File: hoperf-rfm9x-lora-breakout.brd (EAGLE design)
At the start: 26 x 22.5 mm, 6 parts, among them U1 HopeRF-RFM9x

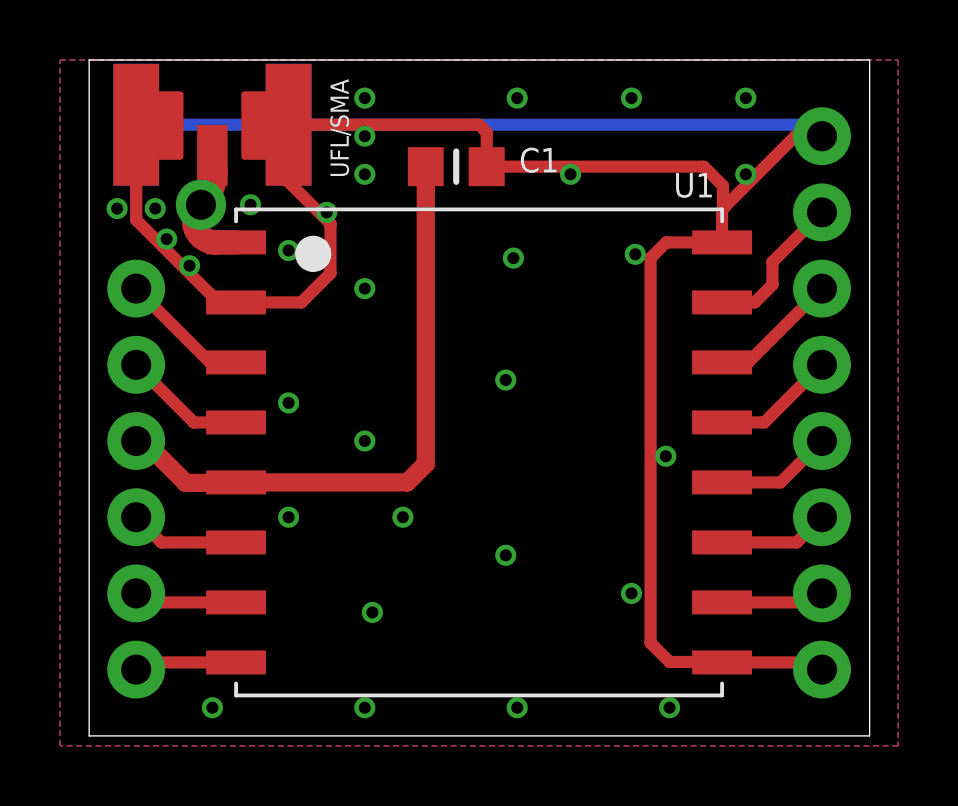
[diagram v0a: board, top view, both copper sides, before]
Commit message: rfm9x lora breakout v1.1
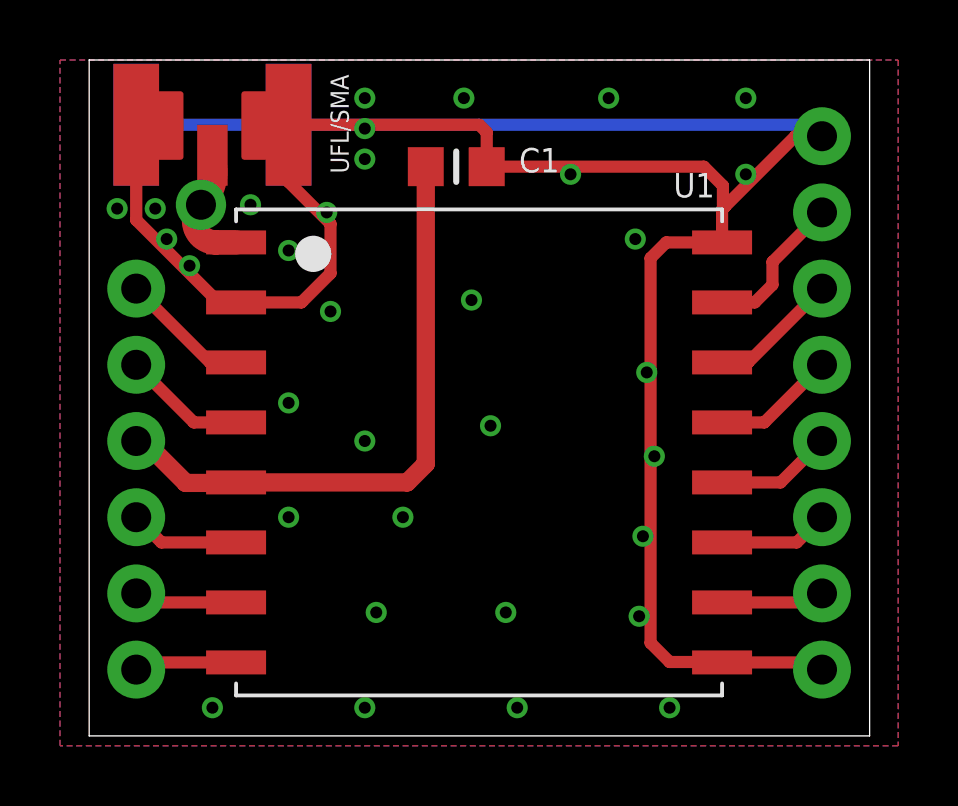
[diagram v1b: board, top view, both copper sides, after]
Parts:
- added LOGO1: OSHW-LOGOS, SparkFun-Aesthetics:OSHW-LOGO-S
- added U$3: LORA_LOGO, #afb-Aesthetics:LORA_LOGO
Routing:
- net GND: vias 31 -> 33
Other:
- board text added: "ANT"
- board text added: "Freq: 315 ( ) 433 ( ) 868 ( ) 915 ( )"
- board text added: "github.com/altro-id"
- board text removed: "Freq: 433 ( ) 868 ( ) 915 ( )"
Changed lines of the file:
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@@
 <setting verticaltext="up"/>
 </settings>
-<grid distance="0.025" unitdist="inch" unit="inch" style="lines" multiple="1" display="no" altdistance="0.025" altunitdist="inch" altunit="inch"/>
+<grid distance="0.005" unitdist="inch" unit="inch" style="lines" multiple="1" display="no" altdistance="0.025" altunitdist="inch" altunit="inch"/>
 <layers>
 <layer number="1" name="Top" color="4" fill="1" visible="yes" active="yes"/>
@@
 <wire x1="0.9725" y1="0.33" x2="26.9875" y2="0.33" width="0" layer="20"/>
 <wire x1="26.9875" y1="0.33" x2="26.9875" y2="22.86" width="0" layer="20"/>
-<text x="19.558" y="13.081" size="0.8128" layer="26" font="vector" ratio="18" rot="MR0">HopeRF-RFM9x
+<text x="18.288" y="12.065" size="0.8128" layer="26" font="vector" ratio="18" rot="MR0">HopeRF-RFM9x
 LoRa Module</text>
-<text x="19.558" y="8.001" size="0.8128" layer="26" font="vector" ratio="18" rot="MR0">Freq:
+<text x="18.288" y="5.207" size="0.8128" layer="26" font="vector" ratio="18" rot="MR0">Freq:
+315 (  )
 433 (  )
 868 (  )
 915 (  )</text>
-<text x="-1.27" y="15.24" size="1.27" layer="103" align="center-right">DIO3</text>
-<text x="-1.27" y="12.7" size="1.27" layer="103" align="center-right">DIO4</text>
-<text x="-1.27" y="10.16" size="1.27" layer="103" align="center-right">+3.3V</text>
-<text x="-1.27" y="7.62" size="1.27" layer="103" align="center-right">DIO0</text>
-<text x="-1.27" y="5.08" size="1.27" layer="103" align="center-right">DIO1</text>
-<text x="-1.27" y="2.54" size="1.27" layer="103" align="center-right">DIO2</text>
-<text x="29.21" y="20.32" size="1.27" layer="103" rot="R180" align="center-right">GND</text>
-<text x="29.21" y="17.78" size="1.27" layer="103" rot="R180" align="center-right">DIO5</text>
-<text x="29.21" y="15.24" size="1.27" layer="103" rot="R180" align="center-right">RESET</text>
-<text x="29.21" y="12.7" size="1.27" layer="103" rot="R180" align="center-right">NSS</text>
-<text x="29.21" y="10.16" size="1.27" layer="103" rot="R180" align="center-right">SCK</text>
-<text x="29.21" y="7.62" size="1.27" layer="103" rot="R180" align="center-right">MOSI</text>
-<text x="29.21" y="5.08" size="1.27" layer="103" rot="R180" align="center-right">MISO</text>
-<text x="29.21" y="2.54" size="1.27" layer="103" rot="R180" align="center-right">GND</text>
+<text x="4.064" y="15.24" size="0.8128" layer="26" font="vector" ratio="18" rot="MR0" align="center-right">DIO3</text>
+<text x="4.064" y="12.7" size="0.8128" layer="26" font="vector" ratio="18" rot="MR0" align="center-right">DIO4</text>
+<text x="4.064" y="10.16" size="0.8128" layer="26" font="vector" ratio="18" rot="MR0" align="center-right">+3.3V</text>
+<text x="4.064" y="7.62" size="0.8128" layer="26" font="vector" ratio="18" rot="MR0" align="center-right">DIO0</text>
+<text x="4.064" y="5.08" size="0.8128" layer="26" font="vector" ratio="18" rot="MR0" align="center-right">DIO1</text>
+<text x="4.064" y="2.54" size="0.8128" layer="26" font="vector" ratio="18" rot="MR0" align="center-right">DIO2</text>
+<text x="23.876" y="20.32" size="0.8128" layer="26" font="vector" ratio="18" rot="MR180" align="center-right">GND</text>
+<text x="23.876" y="17.78" size="0.8128" layer="26" font="vector" ratio="18" rot="MR180" align="center-right">DIO5</text>
+<text x="23.876" y="15.24" size="0.8128" layer="26" font="vector" ratio="18" rot="MR180" align="center-right">RESET</text>
+<text x="23.876" y="12.7" size="0.8128" layer="26" font="vector" ratio="18" rot="MR180" align="center-right">NSS</text>
+<text x="23.876" y="10.16" size="0.8128" layer="26" font="vector" ratio="18" rot="MR180" align="center-right">SCK</text>
+<text x="23.876" y="7.62" size="0.8128" layer="26" font="vector" ratio="18" rot="MR180" align="center-right">MOSI</text>
+<text x="23.876" y="5.08" size="0.8128" layer="26" font="vector" ratio="18" rot="MR180" align="center-right">MISO</text>
+<text x="23.876" y="2.54" size="0.8128" layer="26" font="vector" ratio="18" rot="MR180" align="center-right">GND</text>
+<text x="13.97" y="1.905" size="0.8128" layer="26" font="vector" ratio="12" rot="MR0" align="bottom-center">github.com/altro-id</text>
+<circle x="4.699" y="18.034" radius="1.1981125" width="0.254" layer="22"/>
+<text x="6.731" y="17.018" size="0.6096" layer="26" font="vector" ratio="15" rot="MR90">ANT</text>
 </plain>
 <attributes>
@@
 <elements>
 <element name="U1" library="#afb-Boards" package="RFM9X_SMT" value="HopeRF-RFM9x" x="13.97" y="9.779" smashed="yes" rot="R180">
-<attribute name="NAME" x="20.448" y="18.279" size="0.8128" layer="25" ratio="18"/>
+<attribute name="NAME" x="20.448" y="18.279" size="0.8128" layer="25" font="vector" ratio="18"/>
 </element>
 <element name="JP1" library="microbuilder" package="1X08_ROUND_76" value="" x="25.4" y="11.43" smashed="yes" rot="R90">
@@
 </element>
 <element name="C1" library="#afb-Passives" package="0805_MP" value="10uF" x="13.208" y="19.304" smashed="yes">
-<attribute name="NAME" x="15.3035" y="19.1135" size="0.8128" layer="25" ratio="18"/>
+<attribute name="NAME" x="15.3035" y="19.1135" size="0.8128" layer="25" font="vector" ratio="18"/>
 <attribute name="VALUE" x="11.6205" y="18.034" size="0.4064" layer="27" ratio="10"/>
 </element>
@@
 </element>
 <element name="UFL/SMA" library="#afb-Connectors" package="MICROBUILDER_SMA_EDGELAUNCH_UFL" value="" x="5.08" y="22.733" smashed="yes" rot="R270">
-<attribute name="NAME" x="9.017" y="22.225" size="0.6096" layer="25" ratio="18" rot="R270"/>
+<attribute name="NAME" x="9.017" y="22.3774" size="0.6096" layer="25" font="vector" ratio="18" rot="R270"/>
 <attribute name="VALUE" x="-1.27" y="17.653" size="0.8128" layer="27" ratio="10" rot="R90"/>
 </element>
+<element name="LOGO1" library="SparkFun-Aesthetics" package="OSHW-LOGO-S" value="OSHW-LOGOS" x="9.652" y="6.477" rot="MR0"/>
+<element name="U$3" library="#afb-Aesthetics" package="LORA_LOGO" value="LORA_LOGO" x="18.923" y="14.478" rot="MR0"/>
 </elements>
 <signals>
@@
 <via x="3.556" y="16.891" extent="1-16" drill="0.4"/>
 <via x="4.318" y="16.002" extent="1-16" drill="0.4"/>
-<via x="15.24" y="21.59" extent="1-16" drill="0.4"/>
-<via x="19.05" y="21.59" extent="1-16" drill="0.4"/>
+<via x="13.462" y="21.59" extent="1-16" drill="0.4"/>
+<via x="18.288" y="21.59" extent="1-16" drill="0.4"/>
 <via x="22.86" y="21.59" extent="1-16" drill="0.4"/>
 <via x="5.08" y="1.27" extent="1-16" drill="0.4"/>
@@
 <via x="15.24" y="1.27" extent="1-16" drill="0.4"/>
 <via x="20.32" y="1.27" extent="1-16" drill="0.4"/>
-<via x="15.113" y="16.256" extent="1-16" drill="0.4"/>
-<via x="14.859" y="12.192" extent="1-16" drill="0.4"/>
+<via x="13.716" y="14.859" extent="1-16" drill="0.4"/>
+<via x="19.558" y="12.446" extent="1-16" drill="0.4"/>
 <via x="11.43" y="7.62" extent="1-16" drill="0.4"/>
-<via x="19.177" y="16.383" extent="1-16" drill="0.4"/>
-<via x="20.193" y="9.652" extent="1-16" drill="0.4"/>
-<via x="19.05" y="5.08" extent="1-16" drill="0.4"/>
-<via x="14.859" y="6.35" extent="1-16" drill="0.4"/>
-<via x="10.16" y="15.24" extent="1-16" drill="0.4"/>
+<via x="19.177" y="16.891" extent="1-16" drill="0.4"/>
+<via x="19.812" y="9.652" extent="1-16" drill="0.4"/>
+<via x="14.351" y="10.668" extent="1-16" drill="0.4"/>
+<via x="14.859" y="4.445" extent="1-16" drill="0.4"/>
+<via x="9.017" y="14.478" extent="1-16" drill="0.4"/>
 <via x="10.16" y="10.16" extent="1-16" drill="0.4"/>
 <via x="7.62" y="7.62" extent="1-16" drill="0.4"/>
 <via x="7.62" y="16.51" extent="1-16" drill="0.4"/>
 <via x="7.62" y="11.43" extent="1-16" drill="0.4"/>
-<via x="10.16" y="20.32" extent="1-16" drill="0.4"/>
+<via x="10.16" y="20.574" extent="1-16" drill="0.4"/>
 <via x="17.018" y="19.05" extent="1-16" drill="0.4"/>
 <via x="22.86" y="19.05" extent="1-16" drill="0.4"/>
 <via x="10.16" y="21.59" extent="1-16" drill="0.4"/>
-<via x="10.16" y="19.05" extent="1-16" drill="0.4"/>
+<via x="10.16" y="19.558" extent="1-16" drill="0.4"/>
 <via x="8.89" y="17.78" extent="1-16" drill="0.4"/>
 <via x="1.905" y="17.907" extent="1-16" drill="0.4"/>
-<via x="10.414" y="4.445" extent="1-16" drill="0.4"/>
+<via x="19.304" y="4.318" extent="1-16" drill="0.4"/>
+<via x="19.431" y="6.985" extent="1-16" drill="0.4"/>
+<via x="10.541" y="4.445" extent="1-16" drill="0.4"/>
 </signal>
 <signal name="MISO">
